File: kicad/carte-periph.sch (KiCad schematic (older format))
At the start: 33 parts, among them J1 PDB, J2 PWR_IN, J3 PROG, J4 Fix, J5 Fix, J6 Fix, J7 Fix, J8 I2C, J9 I2C, U1 PIC24FJ128GA202, U2 Shield_gauche, U3 Shield_droit, Y1 10MHz

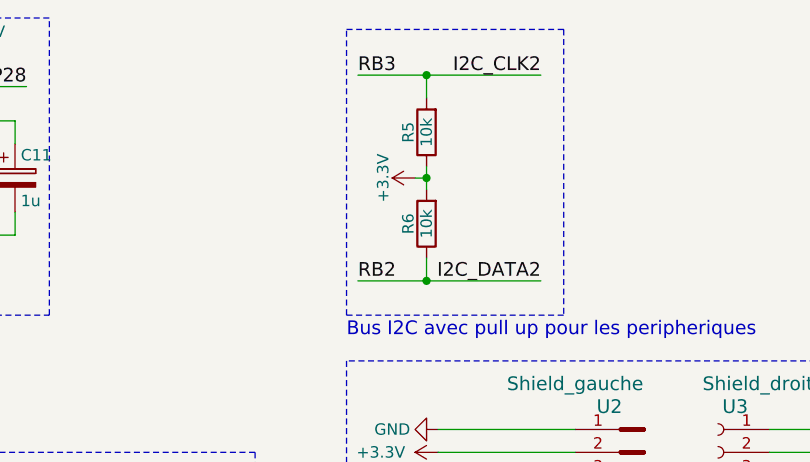
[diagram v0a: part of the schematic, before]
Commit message: Enlèvement des résistances de pull up I2C
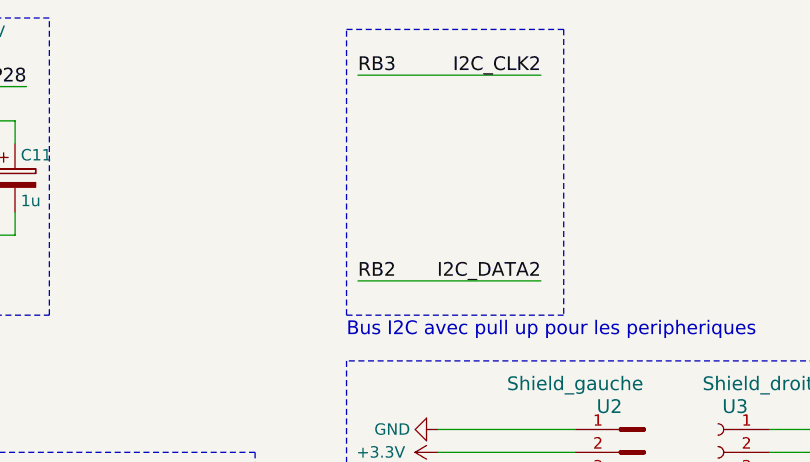
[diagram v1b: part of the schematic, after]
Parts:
- removed R5, R6: 10k, Resistors_THT:R_Axial_DIN0204_L3.6mm_D1.6mm_P7.62mm_Horizontal, symbol R
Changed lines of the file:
@@
 LIBS:conn_shield_1
 LIBS:conn_shield_2
+LIBS:carte-periph-cache
 EELAYER 25 0
 EELAYER END
@@
 Text Label 3100 2650 0    60   ~ 0
 RA4
-Text Label 6650 850  0    60   ~ 0
-RB3
-Text Label 6650 1750 0    60   ~ 0
-RB2
-Text Label 7450 850  2    60   ~ 0
-I2C_CLK2
-Text Label 7450 1750 2    60   ~ 0
-I2C_DATA2
 Text Label 7050 2900 0    60   ~ 0
 RB4
@@
 RB15
 $Comp
-L R R6
-U 1 1 5A9FF9E3
-P 6950 1500
-F 0 "R6" V 7030 1500 50  0000 C CNN
-F 1 "10k" V 6950 1500 50  0000 C CNN
-F 2 "Resistors_THT:R_Axial_DIN0204_L3.6mm_D1.6mm_P7.62mm_Horizontal" V 6880 1500 50  0001 C CNN
-F 3 "" H 6950 1500 50  0001 C CNN
-	1    6950 1500
-	-1   0    0    1
-$EndComp
-$Comp
-L +3.3V #PWR025
-U 1 1 5A9FFBB6
-P 6900 1300
-F 0 "#PWR025" H 6900 1150 50  0001 C CNN
-F 1 "+3.3V" H 6900 1440 50  0000 C CNN
-F 2 "" H 6900 1300 50  0001 C CNN
-F 3 "" H 6900 1300 50  0001 C CNN
-	1    6900 1300
-	0    -1   -1   0
-$EndComp
-$Comp
-L R R5
-U 1 1 5A9FFC28
-P 6950 1100
-F 0 "R5" V 7030 1100 50  0000 C CNN
-F 1 "10k" V 6950 1100 50  0000 C CNN
-F 2 "Resistors_THT:R_Axial_DIN0204_L3.6mm_D1.6mm_P7.62mm_Horizontal" V 6880 1100 50  0001 C CNN
-F 3 "" H 6950 1100 50  0001 C CNN
-	1    6950 1100
-	-1   0    0    1
-$EndComp
-$Comp
 L Conn_01x02 J9
 U 1 1 5AA00D03
@@
 	0    1    1    0
 $EndComp
-Text Notes 6600 2000 0    60   ~ 0
-Bus I2C avec pull up pour les peripheriques
 $Comp
 L Conn_01x02 J8
@@
 	3350 2650 3100 2650
 Wire Wire Line
-	6650 850  7450 850
-Wire Wire Line
-	6650 1750 7450 1750
-Wire Wire Line
 	7600 2900 7050 2900
 Wire Wire Line
@@
 Wire Wire Line
 	8450 3000 9000 3000
-Wire Wire Line
-	6950 1250 6950 1350
-Wire Wire Line
-	6950 1300 6900 1300
-Connection ~ 6950 1300
-Wire Wire Line
-	6950 1650 6950 1750
-Connection ~ 6950 1750
-Wire Wire Line
-	6950 950  6950 850
-Connection ~ 6950 850
-Wire Notes Line
-	7550 650  7550 1900
-Wire Notes Line
-	7550 1900 6600 1900
-Wire Notes Line
-	6600 1900 6600 650
-Wire Notes Line
-	6600 650  7550 650
 Wire Wire Line
 	4050 2650 4750 2650
@@
 	-1   0    0    1
 $EndComp
+Wire Notes Line
+	6600 650  7550 650
+Wire Notes Line
+	6600 1900 6600 650
+Wire Notes Line
+	7550 1900 6600 1900
+Wire Notes Line
+	7550 650  7550 1900
+Wire Wire Line
+	6650 1750 7450 1750
+Wire Wire Line
+	6650 850  7450 850
+Text Notes 6600 2000 0    60   ~ 0
+Bus I2C avec pull up pour les peripheriques
+Text Label 7450 1750 2    60   ~ 0
+I2C_DATA2
+Text Label 7450 850  2    60   ~ 0
+I2C_CLK2
+Text Label 6650 1750 0    60   ~ 0
+RB2
+Text Label 6650 850  0    60   ~ 0
+RB3
 $EndSCHEMATC

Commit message: Mise au propre
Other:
- note added: "I2C"
- note removed: "Bus I2C avec pull up pour les peripheriques"
- note removed: "I2C RASPBERRY"
- moved on the sheet: U2, U3

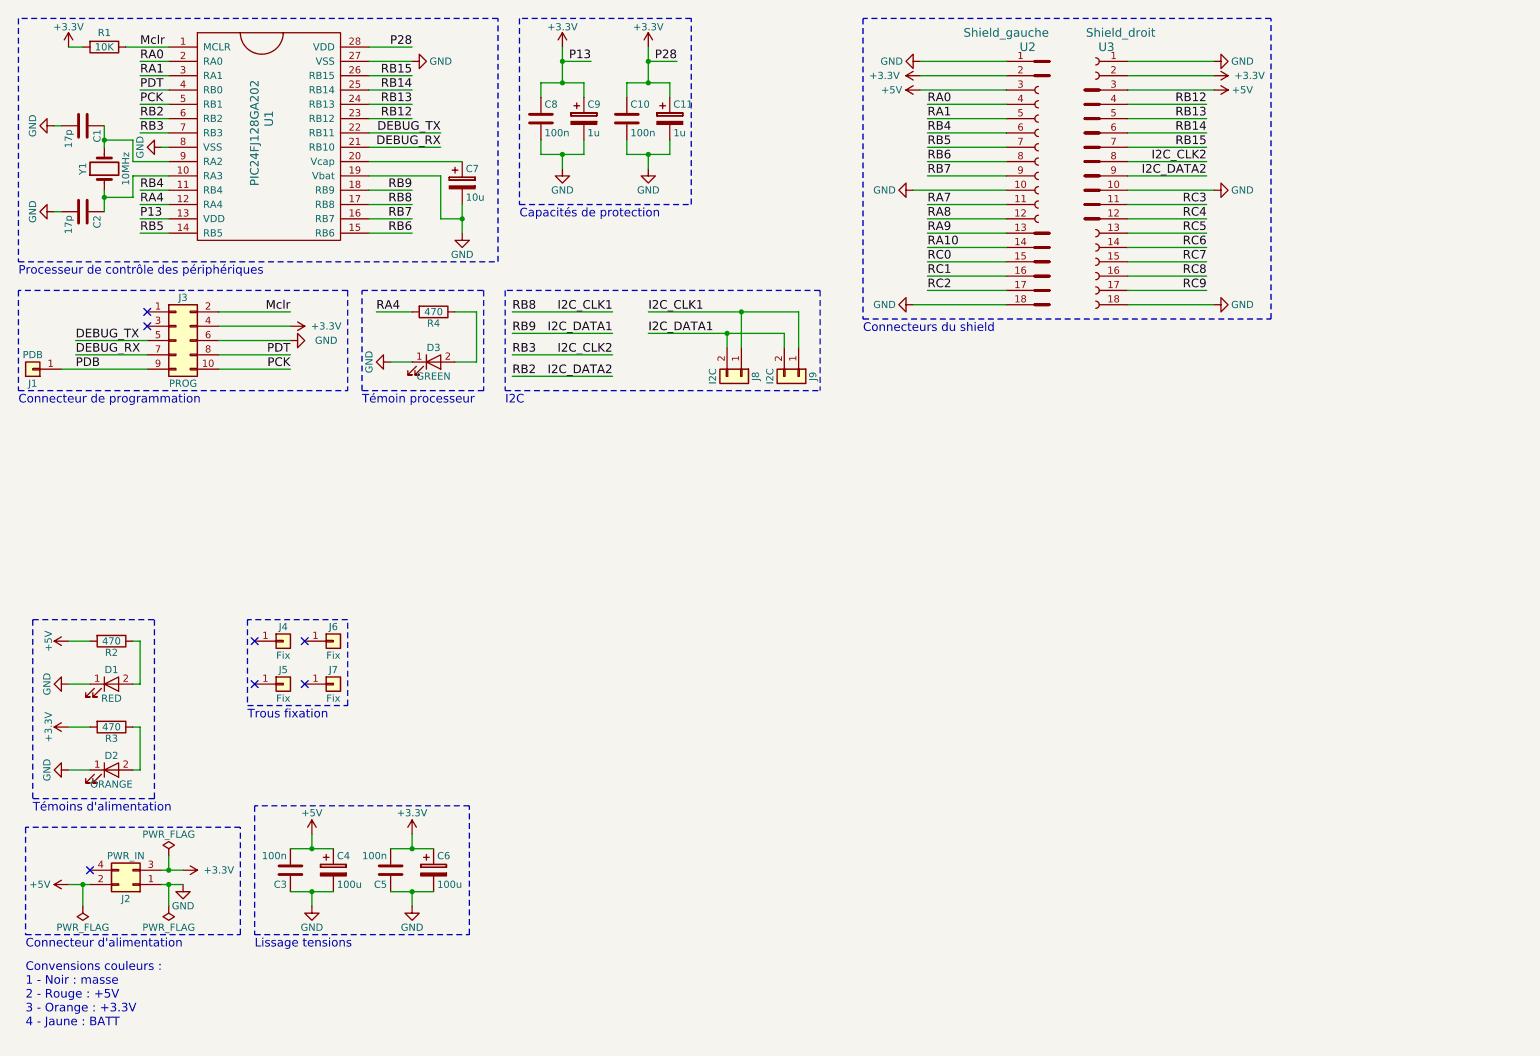
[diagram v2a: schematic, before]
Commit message: Changement du PIC et rajout d'une empreinte de connecteur
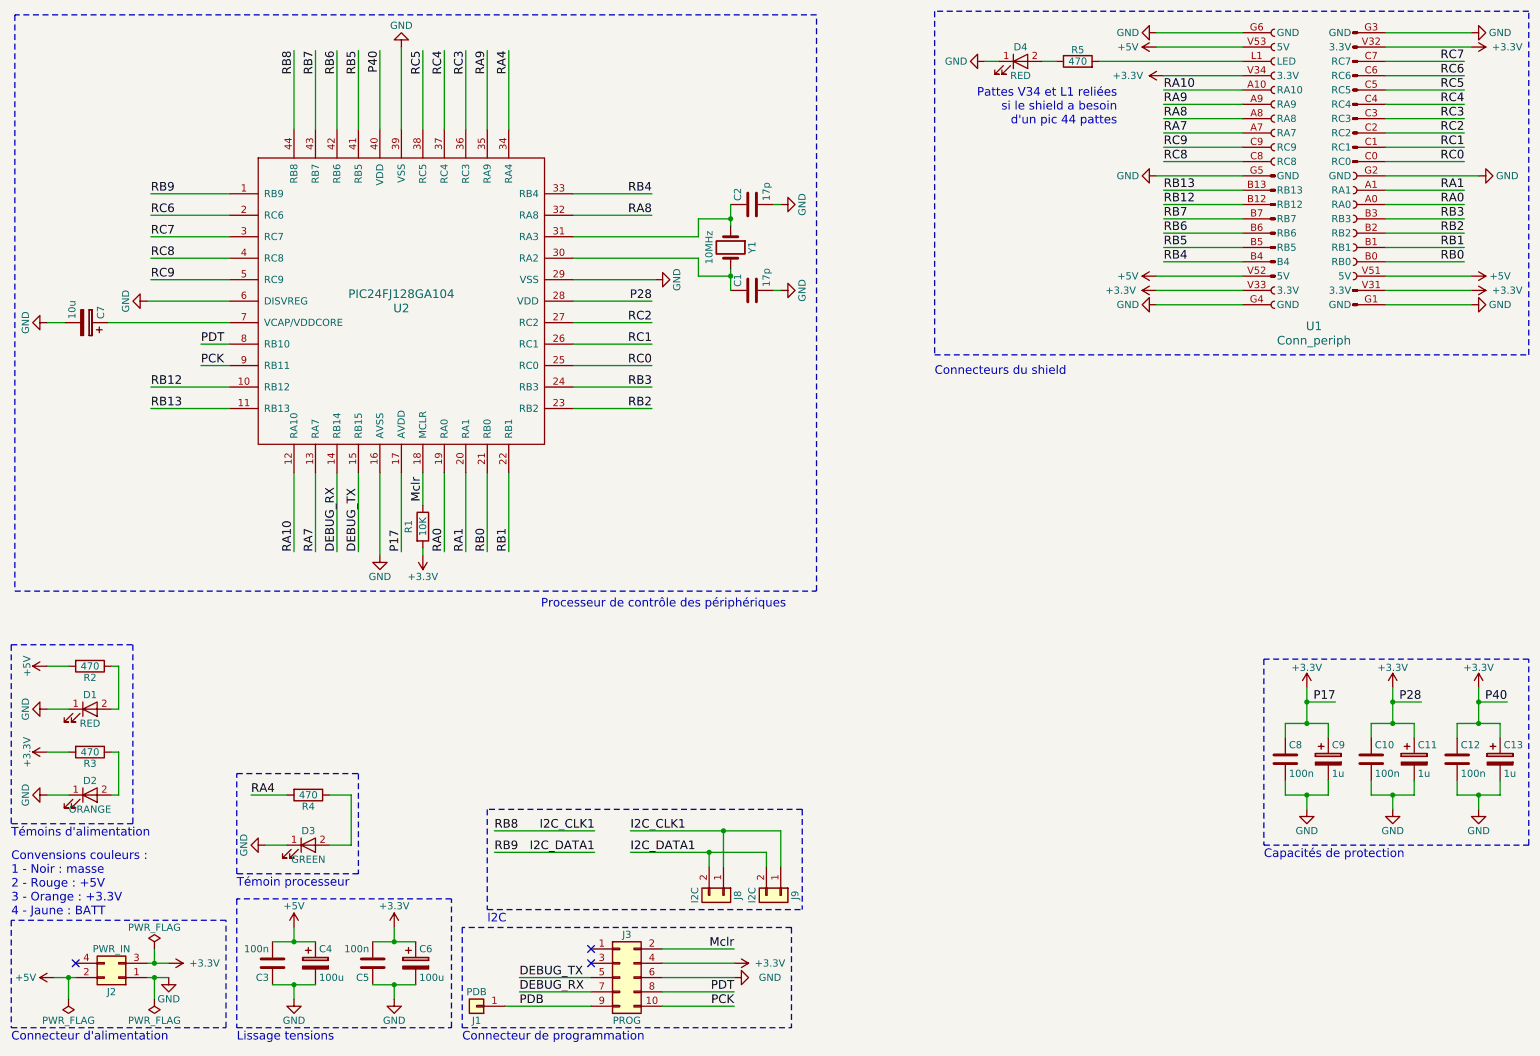
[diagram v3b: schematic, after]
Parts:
- removed J4, J5, J6, J7: Fix, Mounting_Holes:MountingHole_3.2mm_M3_Pad, symbol Conn_01x01
- removed U1: PIC24FJ128GA202, Housings_DIP:DIP-28_W7.62mm, symbol PIC24FJ128GA202
- removed U2: Shield_gauche, conn_shield:conn_shield, symbol Conn_shield_1
- removed U3: Shield_droit, conn_shield:conn_shield, symbol Conn_shield_2
- added C12: 100n, Capacitors_THT:C_Rect_L4.6mm_W2.0mm_P2.50mm_MKS02_FKP02, symbol C
- added C13: 1u, Capacitors_THT:CP_Radial_D5.0mm_P2.50mm, symbol CP
- added D4: RED, LEDs:LED_D3.0mm, symbol LED
- added R5: 470, Resistors_THT:R_Axial_DIN0204_L3.6mm_D1.6mm_P7.62mm_Horizontal, symbol R
- added U1: Conn_periph, conn_periph:conn_periph, symbol Conn_periph
- added U2: PIC24FJ128GA104, Housings_QFP:TQFP-44_10x10mm_Pitch0.8mm, symbol PIC24FJ128GA104
- C1, C10, C2, C3, C5, C8: footprint Capacitors_THT:C_Rect_L7.0mm_W3.5mm_P2.50mm_P5.00mm -> Capacitors_THT:C_Rect_L4.6mm_W2.0mm_P2.50mm_MKS02_FKP02
- C11, C4, C6, C7, C9: footprint Capacitors_THT:CP_Radial_D10.0mm_P2.50mm_P5.00mm -> Capacitors_THT:CP_Radial_D5.0mm_P2.50mm
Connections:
- net +3V3: now also C12.1, C13.1, U1.V31 (3.3V), U1.V32 (3.3V), U1.V33 (3.3V), U1.V34 (3.3V), U2.17 (AVDD), U2.28 (VDD), U2.40 (VDD)
- net +5V: now also U1.V51 (5V), U1.V52 (5V), U1.V53 (5V)
- net DEBUG_RX: now also U2.14 (RB14)
- net DEBUG_TX: now also U2.15 (RB15)
- net GND: now also C12.2, C13.2, D4.1 (K), U1.G1 (GND), U1.G2 (GND), U1.G3 (GND), U1.G4 (GND), U1.G5 (GND), U1.G6 (GND), U2.16 (AVSS), U2.29 (VSS), U2.39 (VSS), U2.6 (DISVREG)
- net I2C_CLK1: now also U2.44 (RB8)
- net I2C_DATA1: now also U2.1 (RB9)
- net Mclr: now also U2.18 (MCLR)
- net PCK: now also U2.9 (RB11)
- net PDT: now also U2.8 (RB10)
- net RA0: now also U1.A0 (RA0), U2.19 (RA0)
- net RA1: now also U1.A1 (RA1), U2.20 (RA1)
- net RA10: now also U1.A10 (RA10), U2.12 (RA10)
- net RA4: now also U2.34 (RA4)
- net RA7: now also U1.A7 (RA7), U2.13 (RA7)
- net RA8: now also U1.A8 (RA8), U2.32 (RA8)
- net RA9: now also U1.A9 (RA9), U2.35 (RA9)
- net RB12: now also U1.B12 (RB12), U2.10 (RB12)
- net RB13: now also U1.B13 (RB13), U2.11 (RB13)
- net RB4: now also U1.B4, U2.33 (RB4)
- net RB5: now also U1.B5 (RB5), U2.41 (RB5)
- net RB6: now also U1.B6 (RB6), U2.42 (RB6)
- net RB7: now also U1.B7 (RB7), U2.43 (RB7)
- net RC0: now also U1.C0 (RC0), U2.25 (RC0)
- net RC1: now also U1.C1 (RC1), U2.26 (RC1)
- net RC2: now also U1.C2 (RC2), U2.27 (RC2)
- net RC3: now also U1.C3 (RC3), U2.36 (RC3)
- net RC4: now also U1.C4 (RC4), U2.37 (RC4)
- net RC5: now also U1.C5 (RC5), U2.38 (RC5)
- net RC6: now also U1.C6 (RC6), U2.2 (RC6)
- net RC7: now also U1.C7 (RC7), U2.3 (RC7)
- net RC8: now also U1.C8 (RC8), U2.4 (RC8)
- net RC9: now also U1.C9 (RC9), U2.5 (RC9)
- net at C7.1: now also U2.7 (VCAP/VDDCORE)
- net at C1.1, Y1.2: now also U2.30 (RA2)
- net at C2.1, Y1.1: now also U2.31 (RA3)
- new net: D4.2 (A), R5.1
- new net: R5.2, U1.L1 (LED)
- new net RB0: U1.B0 (RB0), U2.21 (RB0)
- new net RB1: U1.B1 (RB1), U2.22 (RB1)
- new net RB2: U1.B2 (RB2), U2.23 (RB2)
- new net RB3: U1.B3 (RB3), U2.24 (RB3)
- no-connect marks 7 -> 3
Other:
- note added: "Pattes V34 et L1 reliées\nsi le shield a besoin \nd'un pic 44 pattes"
- note removed: "Trous fixation"
- moved on the sheet: C1, C10, C11, C2, C3, C4, C5, C6, C7, C8, C9, D1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

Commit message: Validation carte, à passer en release
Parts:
- removed D4: RED, LEDs:LED_D3.0mm, symbol LED
- removed R5: 470, Resistors_THT:R_Axial_DIN0204_L3.6mm_D1.6mm_P7.62mm_Horizontal, symbol R
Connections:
- net +3V3: no longer U1.V34 (3.3V)
- no-connect marks 3 -> 5
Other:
- note removed: "Pattes V34 et L1 reliées\nsi le shield a besoin \nd'un pic 44 pattes"
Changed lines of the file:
@@
 Text Label 4625 6425 2    60   ~ 0
-I2C_DATA1
-Text Label 4875 6275 0    60   ~ 0
-I2C_CLK1
-Text Label 4875 6425 0    60   ~ 0
 I2C_DATA1
 Text Notes 3875 6925 0    60   ~ 0
@@
 	9150 1800 8600 1800
 Wire Wire Line
-	3925 6275 4625 6275
-Wire Wire Line
-	3925 6425 4625 6425
-Wire Wire Line
-	4875 6425 5825 6425
+	3925 6275 5925 6275
+Wire Wire Line
+	3925 6425 5825 6425
 Wire Wire Line
 	5425 6425 5425 6525
@@
 Connection ~ 5425 6425
 Wire Wire Line
-	4875 6275 5925 6275
-Wire Wire Line
 	5525 6275 5525 6525
 Wire Wire Line
@@
 	10700 900  10150 900
 Wire Wire Line
-	9150 900  8150 900
-Wire Wire Line
 	8550 1700 9150 1700
 Wire Wire Line
@@
 Wire Wire Line
 	9150 1100 8600 1100
-Wire Wire Line
-	9150 1000 8600 1000
 Wire Wire Line
 	9150 1500 8600 1500
@@
 RB1
 $Comp
-L +3.3V #PWR032
-U 1 1 5ABF9590
-P 8600 1000
-F 0 "#PWR032" H 8600 850 50  0001 C CNN
-F 1 "+3.3V" V 8600 1250 50  0000 C CNN
-F 2 "" H 8600 1000 50  0001 C CNN
-F 3 "" H 8600 1000 50  0001 C CNN
-	1    8600 1000
-	0    -1   -1   0
-$EndComp
-$Comp
-L LED D4
-U 1 1 5ABF9B18
-P 7600 900
-F 0 "D4" H 7600 1000 50  0000 C CNN
-F 1 "RED" H 7600 800 50  0000 C CNN
-F 2 "LEDs:LED_D3.0mm" H 7600 900 50  0001 C CNN
-F 3 "" H 7600 900 50  0001 C CNN
-	1    7600 900
-	1    0    0    -1
-$EndComp
-$Comp
-L R R5
-U 1 1 5ABF9B1E
-P 8000 900
-F 0 "R5" V 8080 900 50  0000 C CNN
-F 1 "470" V 8000 900 50  0000 C CNN
-F 2 "Resistors_THT:R_Axial_DIN0204_L3.6mm_D1.6mm_P7.62mm_Horizontal" V 7930 900 50  0001 C CNN
-F 3 "" H 8000 900 50  0001 C CNN
-	1    8000 900
-	0    -1   -1   0
-$EndComp
-Text Notes 8275 1350 2    60   ~ 0
-Pattes V34 et L1 reliées\nsi le shield a besoin \nd'un pic 44 pattes
-$Comp
 L Conn_periph U1
 U 1 1 5AC0490E
@@
 	0    -1   1    0
 $EndComp
-Wire Wire Line
-	7850 900  7750 900
-$Comp
-L GND #PWR037
-U 1 1 5AC05ACF
-P 7350 900
-F 0 "#PWR037" H 7350 650 50  0001 C CNN
-F 1 "GND" V 7350 700 50  0000 C CNN
-F 2 "" H 7350 900 50  0001 C CNN
-F 3 "" H 7350 900 50  0001 C CNN
-	1    7350 900
-	0    1    -1   0
-$EndComp
-Wire Wire Line
-	7450 900  7350 900
 $Comp
 L PIC24FJ128GA104 U2
@@
 Wire Notes Line
 	575  575  575  4600
+NoConn ~ 9150 900
+NoConn ~ 9150 1000
 $EndSCHEMATC

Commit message: Retouche des connecteurs I2C et ajout du 5V sur le connecteur de programmation
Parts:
- J8, J9: footprint Epsa:KK_2C -> EPSA_KK2C:KK_2C
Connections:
- net +5V: now also J3.3 (Pin_3)
- no-connect marks 5 -> 4
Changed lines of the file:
@@
 $EndDescr
 NoConn ~ 4600 7100
-NoConn ~ 4600 7200
 Text Label 4100 7500 0    60   ~ 0
 PDB
@@
 F 0 "J9" H 5925 6825 50  0000 C CNN
 F 1 "I2C" H 5925 6525 50  0000 C CNN
-F 2 "Epsa:KK_2C" H 5925 6725 50  0001 C CNN
+F 2 "EPSA_KK2C:KK_2C" H 5925 6725 50  0001 C CNN
 F 3 "" H 5925 6725 50  0001 C CNN
 	1    5925 6725
@@
 F 0 "J8" H 5525 6825 50  0000 C CNN
 F 1 "I2C" H 5525 6525 50  0000 C CNN
-F 2 "Epsa:KK_2C" H 5525 6725 50  0001 C CNN
+F 2 "EPSA_KK2C:KK_2C" H 5525 6725 50  0001 C CNN
 F 3 "" H 5525 6725 50  0001 C CNN
 	1    5525 6725
@@
 $EndComp
 $Comp
-L GND #PWR033
+L GND #PWR032
 U 1 1 5AC04C1E
 P 10750 700
-F 0 "#PWR033" H 10750 450 50  0001 C CNN
+F 0 "#PWR032" H 10750 450 50  0001 C CNN
 F 1 "GND" V 10750 500 50  0000 C CNN
 F 2 "" H 10750 700 50  0001 C CNN
@@
 $EndComp
 $Comp
-L +3.3V #PWR034
+L +3.3V #PWR033
 U 1 1 5AC04C24
 P 10750 800
-F 0 "#PWR034" H 10750 650 50  0001 C CNN
+F 0 "#PWR033" H 10750 650 50  0001 C CNN
 F 1 "+3.3V" V 10750 1050 50  0000 C CNN
 F 2 "" H 10750 800 50  0001 C CNN
@@
 	10150 700  10750 700
 $Comp
-L GND #PWR035
+L GND #PWR034
 U 1 1 5AC04F92
 P 8550 700
-F 0 "#PWR035" H 8550 450 50  0001 C CNN
+F 0 "#PWR034" H 8550 450 50  0001 C CNN
 F 1 "GND" V 8550 500 50  0000 C CNN
 F 2 "" H 8550 700 50  0001 C CNN
@@
 	8550 800  9150 800
 $Comp
-L +5V #PWR036
+L +5V #PWR035
 U 1 1 5AC05009
 P 8550 800
-F 0 "#PWR036" H 8550 650 50  0001 C CNN
+F 0 "#PWR035" H 8550 650 50  0001 C CNN
 F 1 "+5V" V 8550 1000 50  0000 C CNN
 F 2 "" H 8550 800 50  0001 C CNN
@@
 	2075 2725 1225 2725
 $Comp
-L GND #PWR038
+L GND #PWR036
 U 1 1 5ACBCCE3
 P 800 2725
-F 0 "#PWR038" H 800 2475 50  0001 C CNN
+F 0 "#PWR036" H 800 2475 50  0001 C CNN
 F 1 "GND" H 800 2575 50  0000 C CNN
 F 2 "" H 800 2725 50  0001 C CNN
@@
 	4475 2425 5050 2425
 $Comp
-L GND #PWR039
+L GND #PWR037
 U 1 1 5ACBE110
 P 5050 2425
-F 0 "#PWR039" H 5050 2175 50  0001 C CNN
+F 0 "#PWR037" H 5050 2175 50  0001 C CNN
 F 1 "GND" H 5050 2275 50  0000 C CNN
 F 2 "" H 5050 2425 50  0001 C CNN
@@
 $EndComp
 $Comp
-L GND #PWR040
+L GND #PWR038
 U 1 1 5ACBE17E
 P 3275 800
-F 0 "#PWR040" H 3275 550 50  0001 C CNN
+F 0 "#PWR038" H 3275 550 50  0001 C CNN
 F 1 "GND" H 3275 650 50  0000 C CNN
 F 2 "" H 3275 800 50  0001 C CNN
@@
 $EndComp
 $Comp
-L GND #PWR041
+L GND #PWR039
 U 1 1 5ACBE29B
 P 3125 4350
-F 0 "#PWR041" H 3125 4100 50  0001 C CNN
+F 0 "#PWR039" H 3125 4100 50  0001 C CNN
 F 1 "GND" H 3125 4200 50  0000 C CNN
 F 2 "" H 3125 4350 50  0001 C CNN
@@
 	2075 2575 1500 2575
 $Comp
-L GND #PWR042
+L GND #PWR040
 U 1 1 5ACC3E91
 P 1500 2575
-F 0 "#PWR042" H 1500 2325 50  0001 C CNN
+F 0 "#PWR040" H 1500 2325 50  0001 C CNN
 F 1 "GND" H 1500 2425 50  0000 C CNN
 F 2 "" H 1500 2575 50  0001 C CNN
@@
 RB1
 $Comp
-L +5V #PWR043
+L +5V #PWR041
 U 1 1 5AA12D34
 P 8550 2400
-F 0 "#PWR043" H 8550 2250 50  0001 C CNN
+F 0 "#PWR041" H 8550 2250 50  0001 C CNN
 F 1 "+5V" V 8550 2600 50  0000 C CNN
 F 2 "" H 8550 2400 50  0001 C CNN
@@
 $EndComp
 $Comp
-L +3.3V #PWR044
+L +3.3V #PWR042
 U 1 1 5ACCCB69
 P 10800 5275
-F 0 "#PWR044" H 10800 5125 50  0001 C CNN
+F 0 "#PWR042" H 10800 5125 50  0001 C CNN
 F 1 "+3.3V" H 10800 5415 50  0000 C CNN
 F 2 "" H 10800 5275 50  0001 C CNN
@@
 $EndComp
 $Comp
-L GND #PWR045
+L GND #PWR043
 U 1 1 5ACCCB6F
 P 10800 6125
-F 0 "#PWR045" H 10800 5875 50  0001 C CNN
+F 0 "#PWR043" H 10800 5875 50  0001 C CNN
 F 1 "GND" H 10800 5975 50  0000 C CNN
 F 2 "" H 10800 6125 50  0001 C CNN
@@
 NoConn ~ 9150 900
 NoConn ~ 9150 1000
+Wire Wire Line
+	4600 7200 4100 7200
+$Comp
+L +5V #PWR044
+U 1 1 5AD9B059
+P 4100 7200
+F 0 "#PWR044" H 4100 7050 50  0001 C CNN
+F 1 "+5V" V 4100 7400 50  0000 C CNN
+F 2 "" H 4100 7200 50  0001 C CNN
+F 3 "" H 4100 7200 50  0001 C CNN
+	1    4100 7200
+	0    -1   -1   0
+$EndComp
 $EndSCHEMATC
